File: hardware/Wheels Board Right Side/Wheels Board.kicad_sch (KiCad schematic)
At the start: 33 parts, among them J1 Conn_01x05, J10 gnd, J11 hall_out, J12 Conn_01x05, J2 24v, J3 Conn_01x03, J4 53307-2471, J6 Conn_01x05_Pin, J7 Conn_01x07, J8 24v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

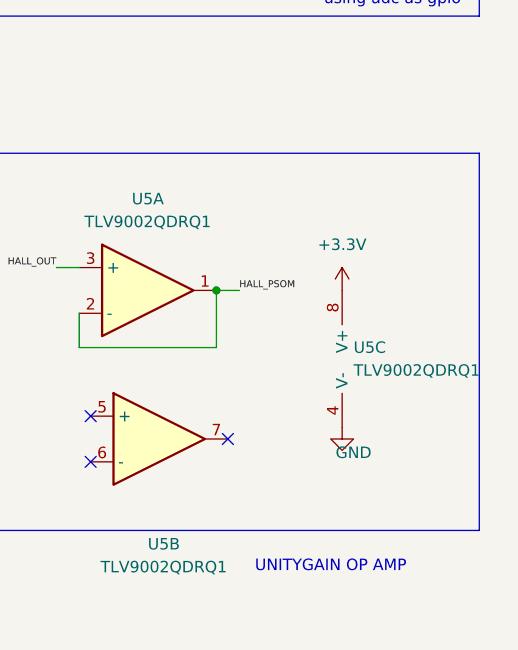
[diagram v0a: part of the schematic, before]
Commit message: changed hall conn, silkscreen fix
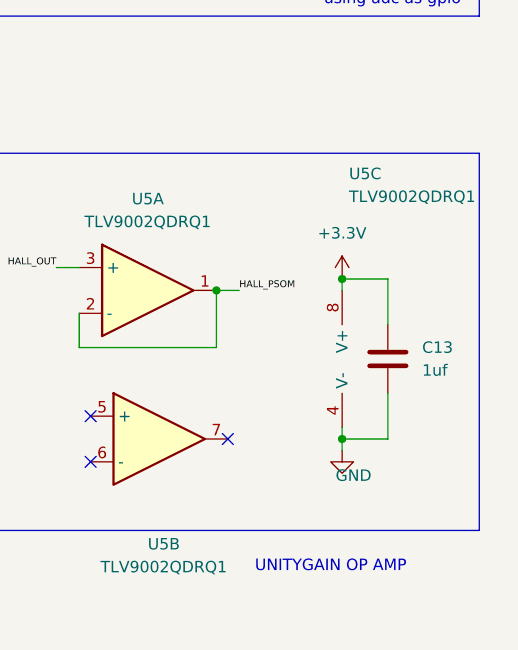
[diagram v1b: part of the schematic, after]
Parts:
- added C13: 1uf, Capacitor_SMD:C_0603_1608Metric_Pad1.08x0.95mm_HandSolder, symbol Device:C
- J3: footprint Connector_PinHeader_2.54mm:PinHeader_1x03_P2.54mm_Horizontal -> Connector_Molex:Molex_Nano-Fit_105313-xx03_1x03_P2.50mm_Horizontal
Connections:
- net +3.3V: now also C13.1
- net GND: now also C13.2
